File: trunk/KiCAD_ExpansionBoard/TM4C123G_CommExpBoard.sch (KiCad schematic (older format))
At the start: 0 parts

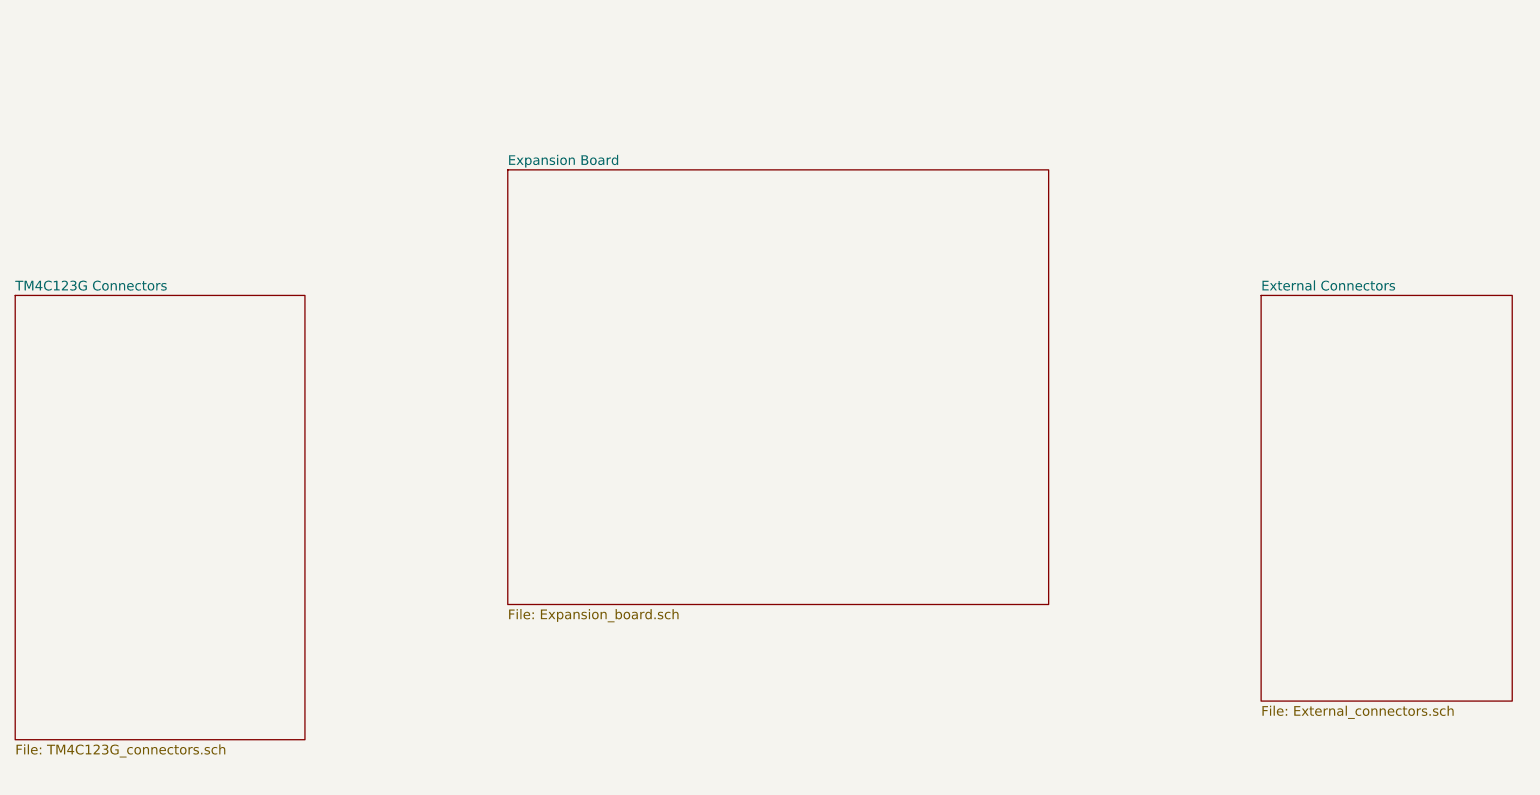
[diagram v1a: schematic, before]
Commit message: Circuit board schematic complete! TODO: Update schematic according new received specifics: "note-expansionboard_20140623.txt"
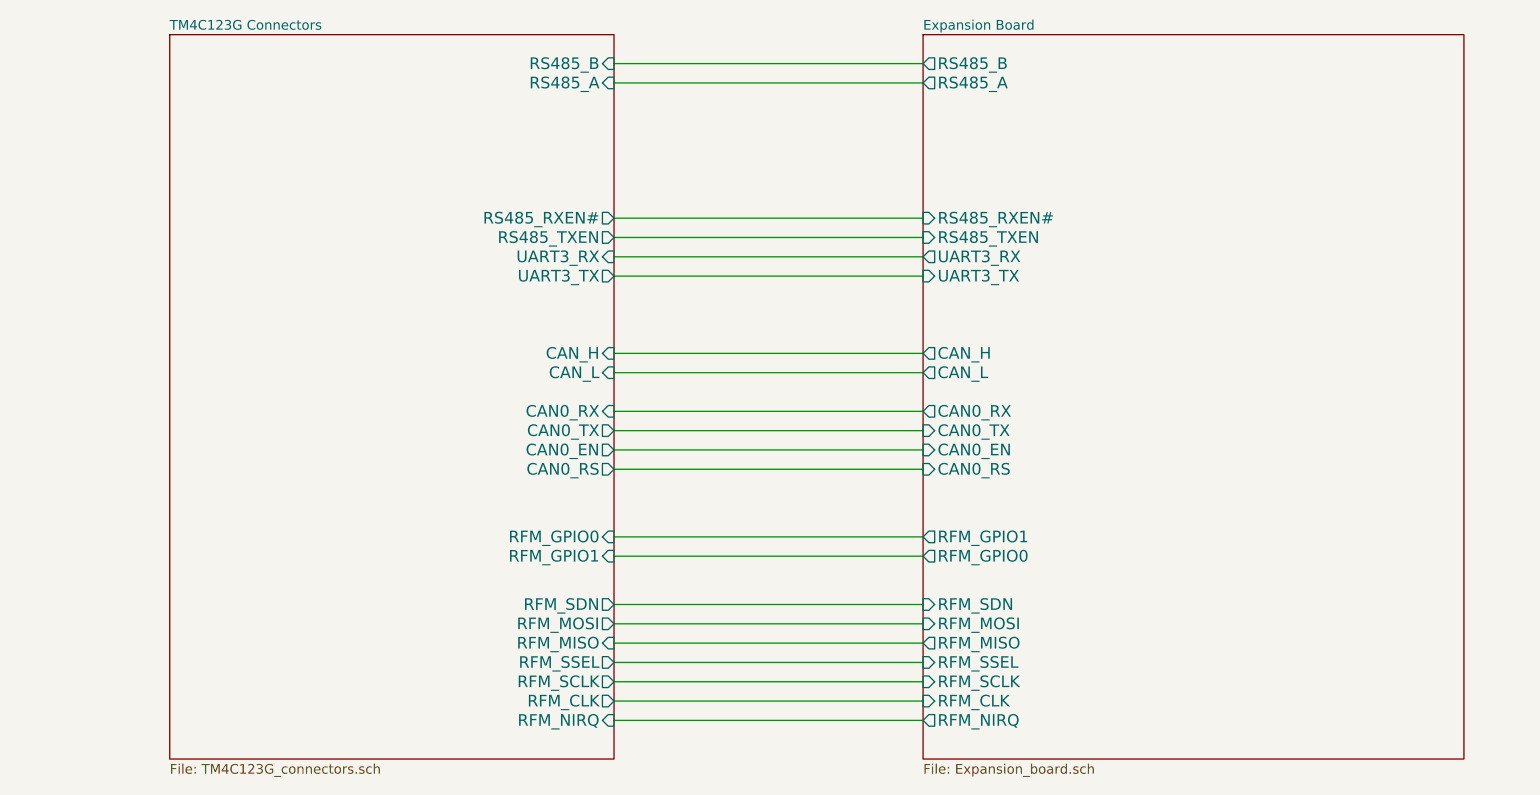
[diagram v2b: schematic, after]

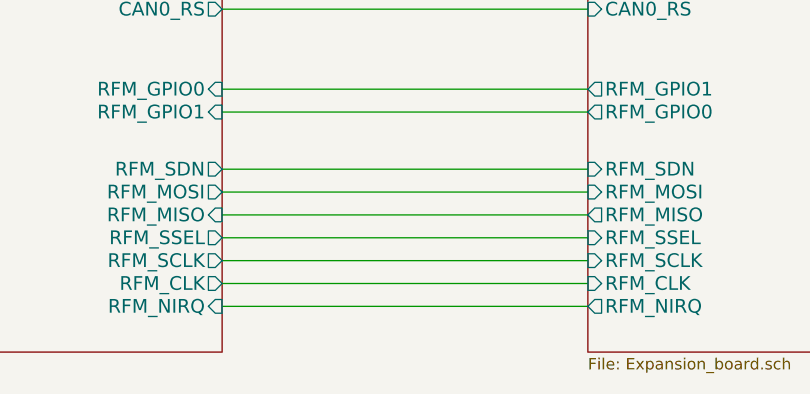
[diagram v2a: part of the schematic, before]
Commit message: -Unito le due linee a 3.3V e riposizionato Q1 che ora va ad interrompere la linea di alimentazione a 3.3V dello switching quando è presente la +5V_TLP (USB). In serie al gate ho messo R8 da 120 ohm e ho lasciato R7 da 10k di pull-down.
-Ho messo un NPN, Q3, che ha al suo interno un partitore da 22k + 47k; è pilotato dalla +5V_TLP ed ho messo R1 verso +12V_BUS che mantiene attivo lo switching a meno che non sia presente la +5V_TLP (Q3 ON). Infine ho posizionato il led a monte del PMOS.

-Per la protezione dalle sovratensioni sulla +5V_TLP ho inserito, all'ingesso, TVS4 che è bidirezionale con tensione di lavoro a 5V e tensione di breakdown di 5.8V (min).

-Rimosse tutte le resistenze di pull-up nei transceiver: ne avevano alcune già internamente.

-Sostituiti gli header-jumper per i terminatori e la rete di fail-safe biasing con un SPDT (SW1), ed un 4PDT (SW2).

In serie al pin RS del transceiver ho messo una 10k.

Pull-up da 10k su SDN dell'RF module
 
Ho inserito un secondo TP P1, ANT_GND che posizionerò vicino al primo, P5, ANT_C per il collegamento dell'antenna.

-MISURA DELLA TENSIONE DI BUS: V_AN_MONITOR: ho ricalcolato i valori di R19 e R20 per ottenere un divider ratio pari a 6.236 circa anziché 6.206 come indicato. La tensione di fondo scala sarà vicina ai 20 V.

-Il TVS3 (SMCJ12CA) indicato è bidirezionale (DS: http://www.farnell.com/datasheets/1794554.pdf), così ho corretto il simbolo mettendone uno appropriato.

-Sostituito lo "spare-function header" da 2x4 pin con uno 2x5 pin reimpostando pin-out come indicato, comprensivo di massa ed alimentazione.
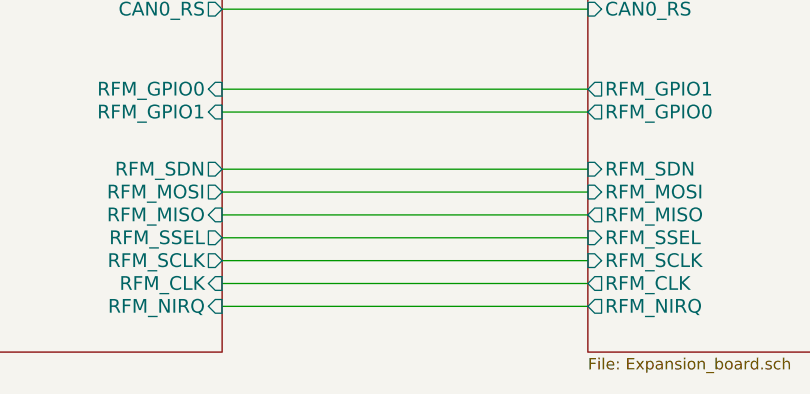
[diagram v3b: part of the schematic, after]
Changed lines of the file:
@@
 LIBS:transceiver
 LIBS:tvs
+LIBS:bid_tvs
 LIBS:TM4C123G_CommExpBoard-cache
 EELAYER 27 0
@@
 Sheet 1 3
 Title "TM4C123G Communication Expansion Board"
-Date "1 jul 2014"
-Rev "0.1"
+Date "3 jul 2014"
+Rev "0.2"
 Comp "Luca Buccolini, Student @ Università Politecnica delle Marche"
 Comment1 "Expansion Board for the Texas Instruments TM4C123G Launchpad "
@@
 F19 "RFM_SSEL" I L 6350 5100 60
 F20 "RFM_SCLK" I L 6350 5200 60
-F21 "RFM_CLK" I L 6350 5300 60
+F21 "RFM_CLK" O L 6350 5300 60
 F22 "RFM_NIRQ" O L 6350 5400 60
 $EndSheet
@@
 F20 "RFM_SSEL" O R 4750 5100 60
 F21 "RFM_SCLK" O R 4750 5200 60
-F22 "RFM_CLK" O R 4750 5300 60
+F22 "RFM_CLK" I R 4750 5300 60
 $EndSheet
 $EndSCHEMATC
